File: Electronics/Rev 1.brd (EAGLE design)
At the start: 101.6 x 101.6 mm, 209 parts, among them P1 5-2301994-4, Q1 BCV27, Q10 BCV26SOT23, Q11 BCV27, Q12 BCV26SOT23, Q13 BCV27, Q14 BCV26SOT23, Q15 BCV27, Q16 BCV26SOT23, Q17 BCV27, Q18 BCV26SOT23, Q19 BCV27, Q2 BCV26SOT23, Q20 BCV26SOT23, Q21 BCV27, Q22 BCV26SOT23, Q23 BCV27, Q24 BCV26SOT23, Q25 PBSS4360XFPBSS4360XF, Q26 MMBT3904,215MMBT3904,215, Q27 PBSS4360XFPBSS4360XF, Q28 MMBT3904,215MMBT3904,215, Q29 PBSS4360XFPBSS4360XF, Q3 BCV27, Q30 TIP35CTIP35C, Q31 PBSS4360XFPBSS4360XF, Q32 MMBT3904,215MMBT3904,215, Q33 TIP35CTIP35C, Q34 PBSS4360XFPBSS4360XF, Q35 MMBT3904,215MMBT3904,215, Q36 MMBT3904,215MMBT3904,215, Q37 MMBT3904,215MMBT3904,215, Q38 MMBT3904,215MMBT3904,215, Q39 MMBT3904,215MMBT3904,215, Q4 BCV26SOT23, Q5 BCV27, Q6 BCV26SOT23, Q7 BCV27, Q8 BCV26SOT23, Q9 BCV27, U1 LFXP6E-3FN256C, U10 RPI, U11 3.3V, U12 3.3V, U13 3.3V, U14 LT1025CN8PBF, U15 LTC1049CS8#PBF, U16 MCP3021A1T-E/OTSOT23, U2 MCP4251, U3 MCP4251, U4 MMA8453QR116QFN, U5 74AHC1G66GW,125TSSOP6, U6 74AHC1G66GW,125TSSOP6, U7 74AHC1G66GW,125TSSOP6, U8 MCP3021A1T-E/OTSOT23, U9 MC74HC164BDR2GMC74HC164BDR2G, Y1 DSC1122B

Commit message: Layed out board
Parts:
- removed JP10: (no value), fillament-winder:1X06
- added C50: 0.1uF, fillament-winder:0805
- added JP13: (no value), fillament-winder:1X03
- added U$4: PCB_CARVER, fillament-winder:PCB_CARVER
- R12, R6: value 10k -> 1M
- moved JP11 469.3 mm to (3.81, 72.4), turned to 270 degrees
- moved R21 463.5 mm to (6.35, 83.8), turned to 90 degrees
- moved R22 461.7 mm to (8.89, 86.4), turned to 0 degrees
- moved JP12 461.6 mm to (7.62, 72.4), turned to 270 degrees
- moved Q36 458.5 mm to (8.89, 83.8), turned to 0 degrees
- moved Q37 456.5 mm to (11.4, 85.1)
- moved R51 454.3 mm to (11.4, 74.9), turned to 0 degrees
- moved R50 453.8 mm to (11.4, 69.8), turned to 0 degrees
- moved R48 453.6 mm to (11.4, 67.3), turned to 0 degrees
- moved R49 453.5 mm to (11.4, 64.8), turned to 0 degrees
- moved R18 450.9 mm to (13.0, 72.4), turned to 180 degrees
- moved C31 449.4 mm to (15.2, 88.9), turned to 0 degrees
- moved R20 448.8 mm to (15.2, 86.4), turned to 180 degrees
- moved C32 448.7 mm to (16.5, 95.2), turned to 0 degrees
- moved R19 448.2 mm to (15.2, 83.8), turned to 180 degrees
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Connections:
- removed net COMM_1N: JP19.2, U1.N12
- removed net COMM_1P: JP19.1, U1.P11
- removed net COMM_2N: JP20.2, U1.R15
- removed net COMM_2P: JP20.1, U1.T15
- removed net COMM_3N: JP21.2, U1.L5
- removed net COMM_3P: JP21.1, U1.K3
- removed net ETH_RX+: P1.P4, R32.P$2, U1.T14
- removed net ETH_RX-: P1.P6, R35.P$2, U1.R14
- removed net ETH_TX+: P1.P1, R30.P$2, U1.R11
- removed net ETH_TX-: P1.P3, R31.P$2, U1.P12
- new net COMM_1_N: JP19.2, U1.R6
- new net COMM_1_P: JP19.1, U1.T6
- new net COMM_2_N: JP20.2, U1.T3
- new net COMM_2_P: JP20.1, U1.R3
- new net COMM_3_N: JP21.2, U1.T2
- new net COMM_3_P: JP21.1, U1.R2
- new net ETH_RX_N: P1.P6, R35.P$2, U1.R15
- new net ETH_RX_P: P1.P4, R32.P$2, U1.T15
- new net ETH_TX_N: P1.P3, R31.P$2, U1.T11
- new net ETH_TX_P: P1.P1, R30.P$2, U1.T10
- new net HEATER_PWR: C14.P$2, C15.P$2, C16.P$2, C17.P$2, JP16.1, JP22.1, JP23.2, JP4.1, JP5.1, Q26.3, Q28.3, R39.P$2
- net +12V: now also C50.P$2
- net +3V3: now also JP13.2; no longer JP10.6, U10.1, U10.17
- net +5V: now also JP13.1
- net ACCEL_INT1: now also U1.A13; no longer JP10.2, U1.T12
- net ACCEL_INT2: now also U1.A12; no longer JP10.1, U1.P13
- net ACCEL_SCL: now also U1.A14; no longer JP10.4, U1.R12
- net ACCEL_SDA: now also U1.A15; no longer JP10.5, U1.M9
- net CLK+: now also U1.H16; no longer U1.G5
- net CLK-: now also U1.J16; no longer U1.L3
- net DAC0_CS: now also U1.F12; no longer U1.R8
- net DAC0_MISO: now also U1.D12; no longer U1.R9
- net DAC0_MOSI: now also U1.B15; no longer U1.T9
- net DAC0_SCLK: now also U1.C13; no longer U1.P9
- net DAC1_CS: now also U1.B5; no longer U1.T10
- net DAC1_MISO: now also U1.A5; no longer U1.R10
- net DAC1_MOSI: now also U1.B6; no longer U1.T11
- net DAC1_SCLK: now also U1.A6; no longer U1.P10
- net EXTERNAL_RX: now also U1.P8; no longer U1.P14
- net EXTERNAL_TX: now also U1.N7; no longer U1.T13
- net FAN_ENCODER: now also U1.A4; no longer U1.N9
- net GND: now also C50.P$1, JP13.3; no longer JP10.3
- net POT_CLK: now also U1.A3; no longer U1.R13
- net POT_SCL: now also U1.A2; no longer U1.M11
- net POT_SDA1: now also U1.D7; no longer U1.N11
- net POT_SDA2: now also U1.D6; no longer U1.N10
- net POT_SDA3: now also U1.D5; no longer U1.M10
- net STEPPER_PWR: no longer C14.P$2, C15.P$2, C16.P$2, C17.P$2, JP16.1, JP22.1, JP23.2, JP4.1, JP5.1, Q26.3, Q28.3, R39.P$2
- net THERMO_SCL: now also U1.B7; no longer U1.J3
- net THERMO_SDA1: now also U1.A8; no longer U1.K5
- net THERMO_SDA2: now also U1.A7; no longer U1.L4
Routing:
- net +3V3: track 122.7 -> 673.3 mm, vias 2 -> 15
- net GND: track 237.8 -> 11.0 mm, vias 16 -> 550
- net +12V: track 0.00 -> 219.3 mm, vias 0 -> 2
- net MOTOR_PWR: track 0.00 -> 133.2 mm
- net +5V: track 0.00 -> 117.6 mm, vias 0 -> 3
- net ACCEL_INT2: track 0.00 -> 102.8 mm
- net ACCEL_INT1: track 0.00 -> 97.5 mm
- net ACCEL_SCL: track 0.00 -> 85.7 mm
- net ACCEL_SDA: track 0.00 -> 76.4 mm
- net THERMO_SCL: track 0.00 -> 75.2 mm
- net THERMO_SDA2: track 0.00 -> 67.0 mm
- net THERMO_SDA1: track 0.00 -> 61.5 mm
- net HEATER_PWR: track 0.00 -> 57.0 mm
- net POT_CLK: track 29.9 -> 83.7 mm
- net POT_SCL: track 48.9 -> 95.7 mm
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- added copper zone on layer 1, net GND
- added copper zone on layer 16, net GND

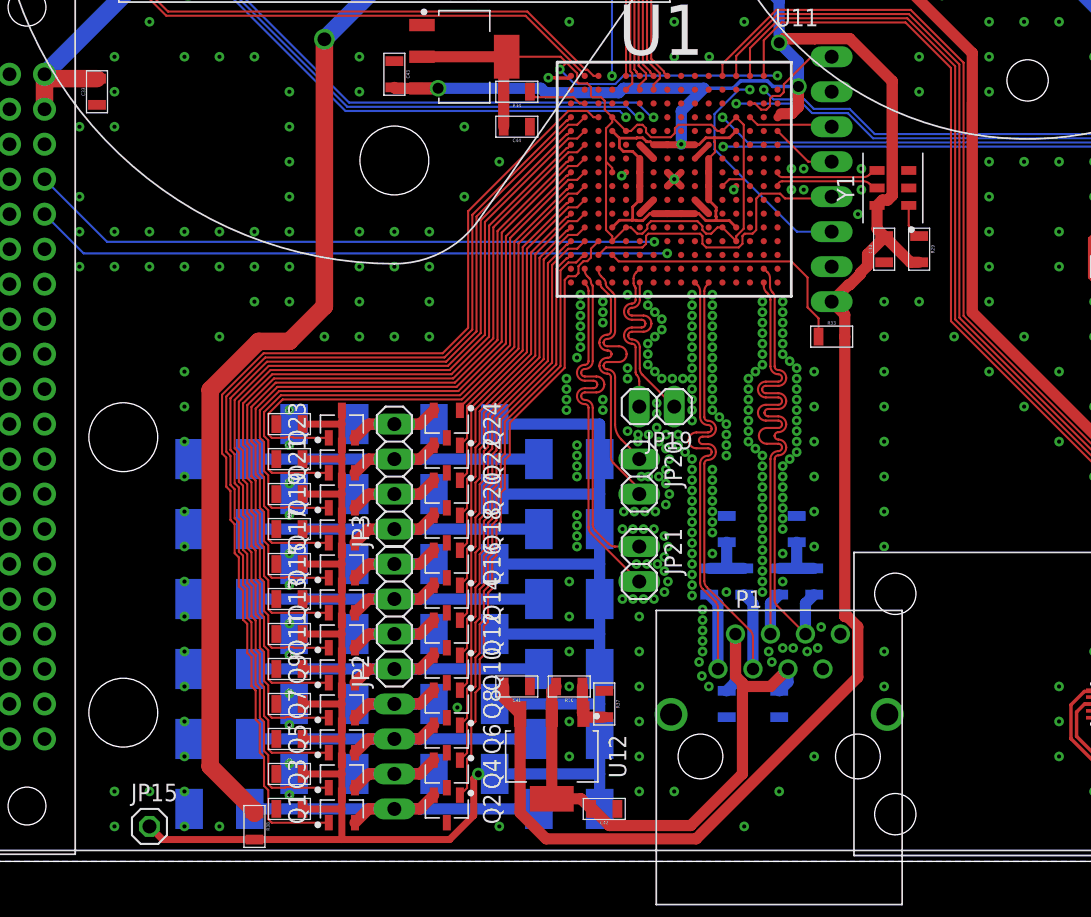
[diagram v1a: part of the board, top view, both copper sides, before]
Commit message: Added GPIO pins
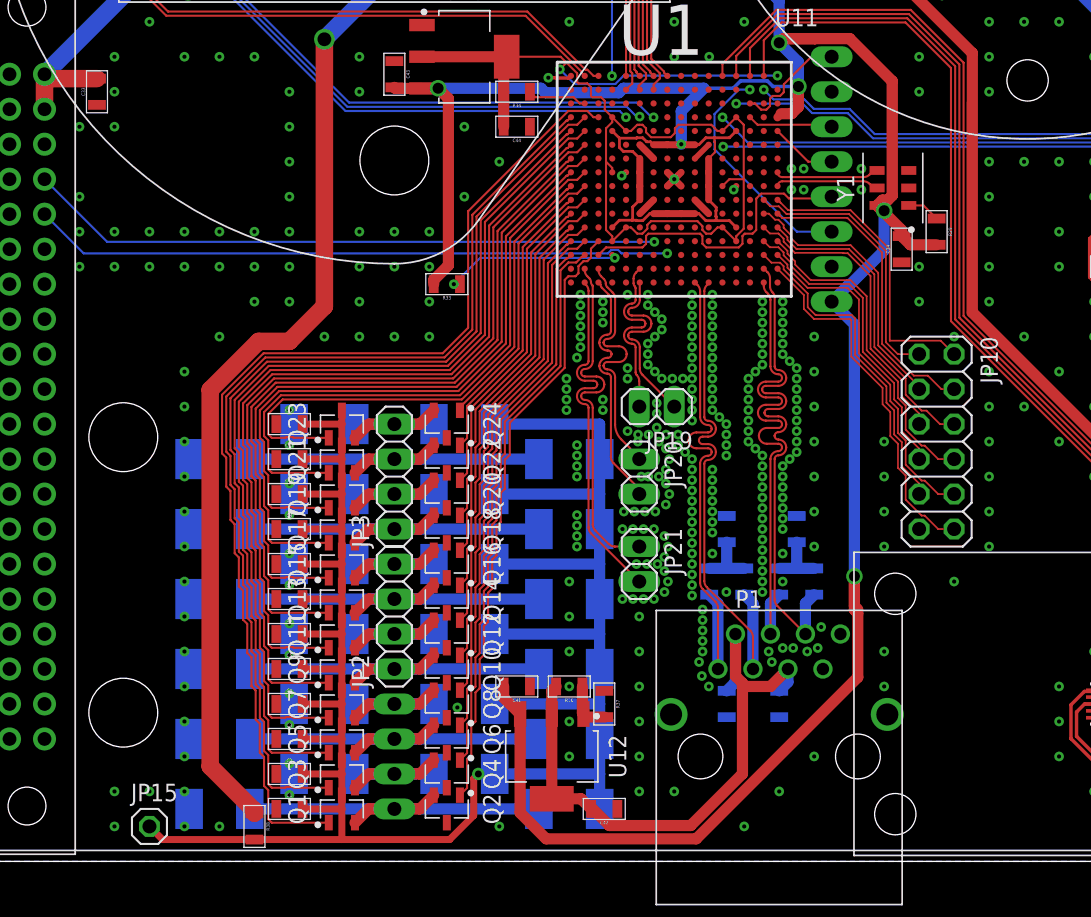
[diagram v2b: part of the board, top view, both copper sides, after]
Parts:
- added JP10: (no value), fillament-winder:2X06
- moved R33 28.2 mm to (34.3, 41.9), turned to 180 degrees
- moved R29 1.80 mm to (69.8, 45.7)
- moved C34 1.27 mm to (67.3, 44.5)
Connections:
- new net GPIO1: JP10.1, U1.K15
- new net GPIO10: JP10.10, U1.P16
- new net GPIO11: JP10.12, U1.R16
- new net GPIO2: JP10.2, U1.K16
- new net GPIO3: JP10.3, U1.L15
- new net GPIO4: JP10.4, U1.L16
- new net GPIO5: JP10.5, U1.M15
- new net GPIO6: JP10.6, U1.M16
- new net GPIO7: JP10.7, U1.N15
- new net GPIO8: JP10.8, U1.N16
- new net GPIO9: JP10.9, U1.P15
- net GND: now also JP10.11
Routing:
- net GPIO11: track 0.00 -> 26.6 mm
- net GPIO10: track 0.00 -> 25.2 mm
- net GPIO9: track 0.00 -> 23.9 mm
- net GPIO8: track 0.00 -> 23.6 mm
- net GPIO6: track 0.00 -> 22.6 mm
- net GPIO7: track 0.00 -> 22.6 mm
- net GPIO4: track 0.00 -> 22.0 mm
- net GPIO5: track 0.00 -> 21.6 mm
- net GPIO2: track 0.00 -> 21.3 mm
- net GPIO3: track 0.00 -> 20.0 mm
- net GPIO1: track 0.00 -> 19.8 mm
- net SLEEPN: track 19.5 -> 13.2 mm, vias 0 -> 2
- net +3V3: track 673.3 -> 672.7 mm, vias 15 -> 17
- net GND: vias 550 -> 553
